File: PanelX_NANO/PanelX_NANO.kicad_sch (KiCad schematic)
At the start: 0 parts

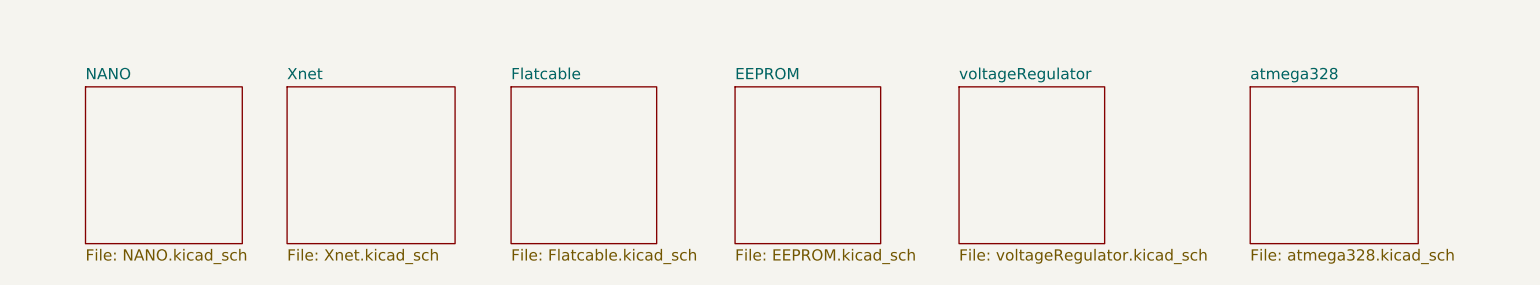
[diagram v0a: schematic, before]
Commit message: Deleted zip files from repo
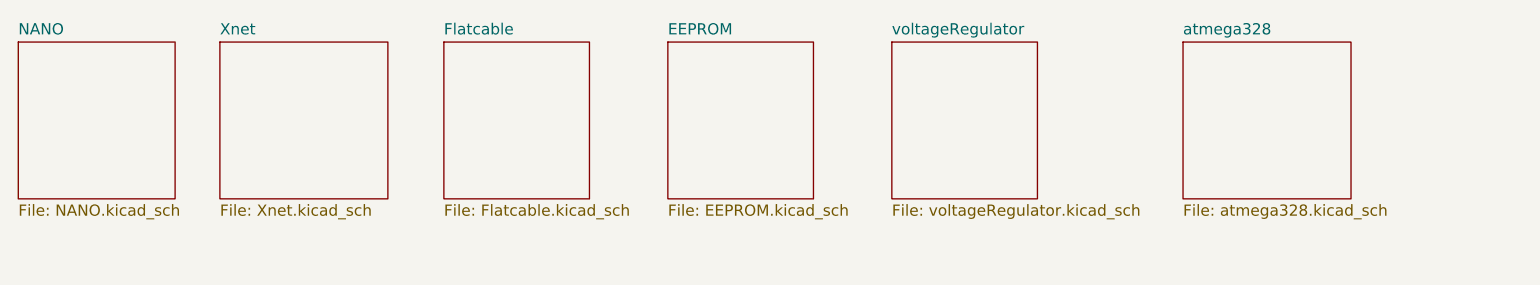
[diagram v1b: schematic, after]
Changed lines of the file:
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@@
 (kicad_sch (version 20211123) (generator eeschema)
   (paper "A4")
-  (sheet (at 45.72 21.59) (size 19.05 17.78) (fields_autoplaced)
+  (sheet (at 38.1 16.51) (size 19.05 17.78) (fields_autoplaced)
     (stroke (width 0.1524) (type solid) (color 0 0 0 0))
     (fill (color 0 0 0 0.0000))
-    (property "Sheet name" "Xnet" (id 0) (at 45.72 20.8784 0)
+    (property "Sheet name" "Xnet" (id 0) (at 38.1 15.7984 0)
       (effects (font (size 1.27 1.27)) (justify left bottom))
     )
-    (property "Sheet file" "Xnet.kicad_sch" (id 1) (at 45.72 39.9546 0)
+    (property "Sheet file" "Xnet.kicad_sch" (id 1) (at 38.1 34.8746 0)
       (effects (font (size 1.27 1.27)) (justify left top))
     )
   )
-  (sheet (at 71.12 21.59) (size 16.51 17.78) (fields_autoplaced)
+  (sheet (at 63.5 16.51) (size 16.51 17.78) (fields_autoplaced)
     (stroke (width 0.1524) (type solid) (color 0 0 0 0))
     (fill (color 0 0 0 0.0000))
-    (property "Sheet name" "Flatcable" (id 0) (at 71.12 20.8784 0)
+    (property "Sheet name" "Flatcable" (id 0) (at 63.5 15.7984 0)
       (effects (font (size 1.27 1.27)) (justify left bottom))
     )
-    (property "Sheet file" "Flatcable.kicad_sch" (id 1) (at 71.12 39.9546 0)
+    (property "Sheet file" "Flatcable.kicad_sch" (id 1) (at 63.5 34.8746 0)
       (effects (font (size 1.27 1.27)) (justify left top))
     )
   )
-  (sheet (at 96.52 21.59) (size 16.51 17.78) (fields_autoplaced)
+  (sheet (at 88.9 16.51) (size 16.51 17.78) (fields_autoplaced)
     (stroke (width 0.1524) (type solid) (color 0 0 0 0))
     (fill (color 0 0 0 0.0000))
-    (property "Sheet name" "EEPROM" (id 0) (at 96.52 20.8784 0)
+    (property "Sheet name" "EEPROM" (id 0) (at 88.9 15.7984 0)
       (effects (font (size 1.27 1.27)) (justify left bottom))
     )
-    (property "Sheet file" "EEPROM.kicad_sch" (id 1) (at 96.52 39.9546 0)
+    (property "Sheet file" "EEPROM.kicad_sch" (id 1) (at 88.9 34.8746 0)
       (effects (font (size 1.27 1.27)) (justify left top))
     )
   )
-  (sheet (at 121.92 21.59) (size 16.51 17.78) (fields_autoplaced)
+  (sheet (at 114.3 16.51) (size 16.51 17.78) (fields_autoplaced)
     (stroke (width 0.1524) (type solid) (color 0 0 0 0))
     (fill (color 0 0 0 0.0000))
-    (property "Sheet name" "voltageRegulator" (id 0) (at 121.92 20.8784 0)
+    (property "Sheet name" "voltageRegulator" (id 0) (at 114.3 15.7984 0)
       (effects (font (size 1.27 1.27)) (justify left bottom))
     )
-    (property "Sheet file" "voltageRegulator.kicad_sch" (id 1) (at 121.92 39.9546 0)
+    (property "Sheet file" "voltageRegulator.kicad_sch" (id 1) (at 114.3 34.8746 0)
       (effects (font (size 1.27 1.27)) (justify left top))
     )
   )
-  (sheet (at 154.94 21.59) (size 19.05 17.78) (fields_autoplaced)
+  (sheet (at 147.32 16.51) (size 19.05 17.78) (fields_autoplaced)
     (stroke (width 0.1524) (type solid) (color 0 0 0 0))
     (fill (color 0 0 0 0.0000))
-    (property "Sheet name" "atmega328" (id 0) (at 154.94 20.8784 0)
+    (property "Sheet name" "atmega328" (id 0) (at 147.32 15.7984 0)
       (effects (font (size 1.27 1.27)) (justify left bottom))
     )
-    (property "Sheet file" "atmega328.kicad_sch" (id 1) (at 154.94 39.9546 0)
+    (property "Sheet file" "atmega328.kicad_sch" (id 1) (at 147.32 34.8746 0)
       (effects (font (size 1.27 1.27)) (justify left top))
     )
   )
-  (sheet (at 22.86 21.59) (size 17.78 17.78) (fields_autoplaced)
+  (sheet (at 15.24 16.51) (size 17.78 17.78) (fields_autoplaced)
     (stroke (width 0.1524) (type solid) (color 0 0 0 0))
     (fill (color 0 0 0 0.0000))
-    (property "Sheet name" "NANO" (id 0) (at 22.86 20.8784 0)
+    (property "Sheet name" "NANO" (id 0) (at 15.24 15.7984 0)
       (effects (font (size 1.27 1.27)) (justify left bottom))
     )
-    (property "Sheet file" "NANO.kicad_sch" (id 1) (at 22.86 39.9546 0)
+    (property "Sheet file" "NANO.kicad_sch" (id 1) (at 15.24 34.8746 0)
       (effects (font (size 1.27 1.27)) (justify left top))
     )

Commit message: I picked a suitable connector. I will use plain 2x12 female n male connectors for the b2b connector. Death to flatcables! The RJ12 connector still goed on the panel carrier board. I will look for vertical SMD variant
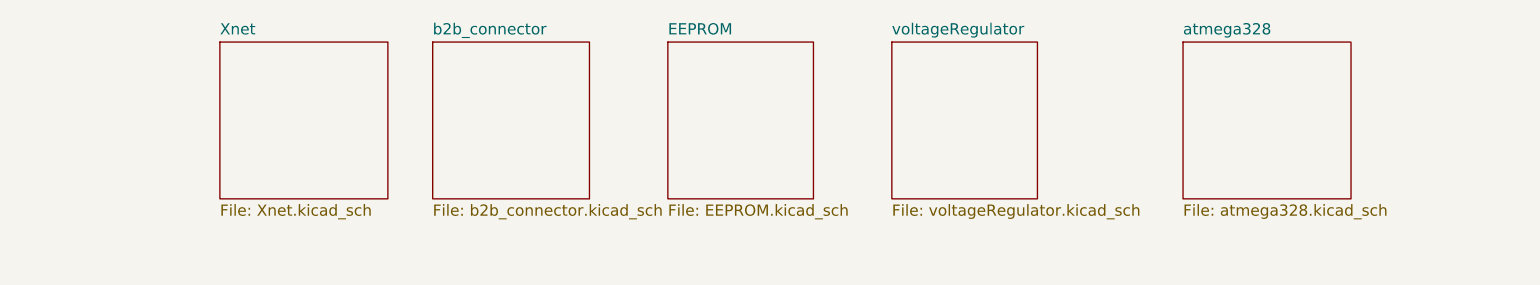
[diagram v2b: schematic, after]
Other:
- removed sheet Flatcable
- removed sheet NANO
- added sheet b2b_connector (b2b_connector.kicad_sch)
